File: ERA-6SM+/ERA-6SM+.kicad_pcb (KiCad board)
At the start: 2 copper layers, 60 x 30 mm, 91 parts, among them P1 CONN_01X02, U1 ERA-6+, X1 SMA-F, X2 SMA-F

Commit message: ERA-6SM+: Changed from 12V supply to 10V
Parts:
- R1: value 100 / 1W -> 69,8 / 0.5W
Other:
- board text added: "10V"
- board text removed: "12V"
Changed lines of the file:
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@@
 (kicad_pcb (version 4) (host pcbnew 4.0.2+e4-6225~38~ubuntu15.10.1-stable)
   (general
-    (links 99)
+    (links 97)
     (no_connects 0)
     (area 82.442143 88.535 180.275002 121.315)
@@
       (effects (font (size 1 1) (thickness 0.15)))
     )
-    (fp_text value "100 / 1W" (at 0 0) (layer F.Fab)
+    (fp_text value "69,8 / 0.5W" (at 0 0) (layer F.Fab)
       (effects (font (size 1 1) (thickness 0.15)))
     )
@@
       (net 1 GNDA))
   )
-  (gr_text 12V (at 112.38 111.223) (layer F.SilkS)
+  (gr_text 10V (at 112.38 111.223) (layer F.SilkS)
     (effects (font (size 1.5 1.5) (thickness 0.3)) (justify right))
   )

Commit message: ERA-6SM+: Table for bias resistor selection
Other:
- board text added: "43.2 69.8 100 127"
- board text added: "8 10 12 14"
- board text added: "R1"
- board text added: "VCC"
- board text removed: "10V"
- board text removed: "Leibniz Universität Hannover, GEM (EMV)"
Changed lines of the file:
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@@
     (area 82.442143 88.535 180.275002 121.315)
     (thickness 1.6)
-    (drawings 13)
+    (drawings 22)
     (tracks 18)
     (zones 0)
@@
     (tags "resistor 1206")
     (attr smd)
-    (fp_text reference R1 (at 3.302 0) (layer F.SilkS)
+    (fp_text reference R1 (at -0.127 2.032) (layer F.SilkS)
       (effects (font (size 1 1) (thickness 0.15)))
     )
@@
       (net 1 GNDA))
   )
-  (gr_text 10V (at 112.38 111.223) (layer F.SilkS)
+  (gr_text "8\n10\n12\n14" (at 128.255 113.89) (layer F.SilkS)
+    (effects (font (size 1 1) (thickness 0.15)) (justify left))
+  )
+  (gr_line (start 127.62 117.7) (end 136.51 117.7) (layer F.SilkS) (width 0.1))
+  (gr_line (start 127.62 110.08) (end 136.51 110.08) (layer F.SilkS) (width 0.1))
+  (gr_line (start 127.62 107.54) (end 136.51 107.54) (layer F.SilkS) (width 0.1))
+  (gr_line (start 136.51 107.54) (end 136.51 117.7) (layer F.SilkS) (width 0.1))
+  (gr_line (start 127.62 107.54) (end 127.62 117.7) (layer F.SilkS) (width 0.1))
+  (gr_line (start 132.065 107.54) (end 132.065 117.7) (layer F.SilkS) (width 0.1))
+  (gr_text "43.2\n69.8\n100\n127" (at 135.875 113.89) (layer F.SilkS)
+    (effects (font (size 1 1) (thickness 0.15)) (justify right))
+  )
+  (gr_text VCC (at 135.875 108.81) (layer F.SilkS)
+    (effects (font (size 1 1) (thickness 0.15)) (justify right))
+  )
+  (gr_text R1 (at 128.255 108.81) (layer F.SilkS)
+    (effects (font (size 1 1) (thickness 0.15)) (justify left))
+  )
+  (gr_text VCC (at 112.38 111.223) (layer F.SilkS)
     (effects (font (size 1.5 1.5) (thickness 0.3)) (justify right))
   )
@@
     (effects (font (size 1 1) (thickness 0.15)) (justify right))
   )
-  (gr_text "Leibniz Universität Hannover, GEM (EMV)" (at 120 117.446) (layer F.SilkS)
-    (effects (font (size 1 1) (thickness 0.15) italic))
-  )
   (gr_text ERA-6SM+ (at 100.1626 94.1796) (layer F.SilkS)

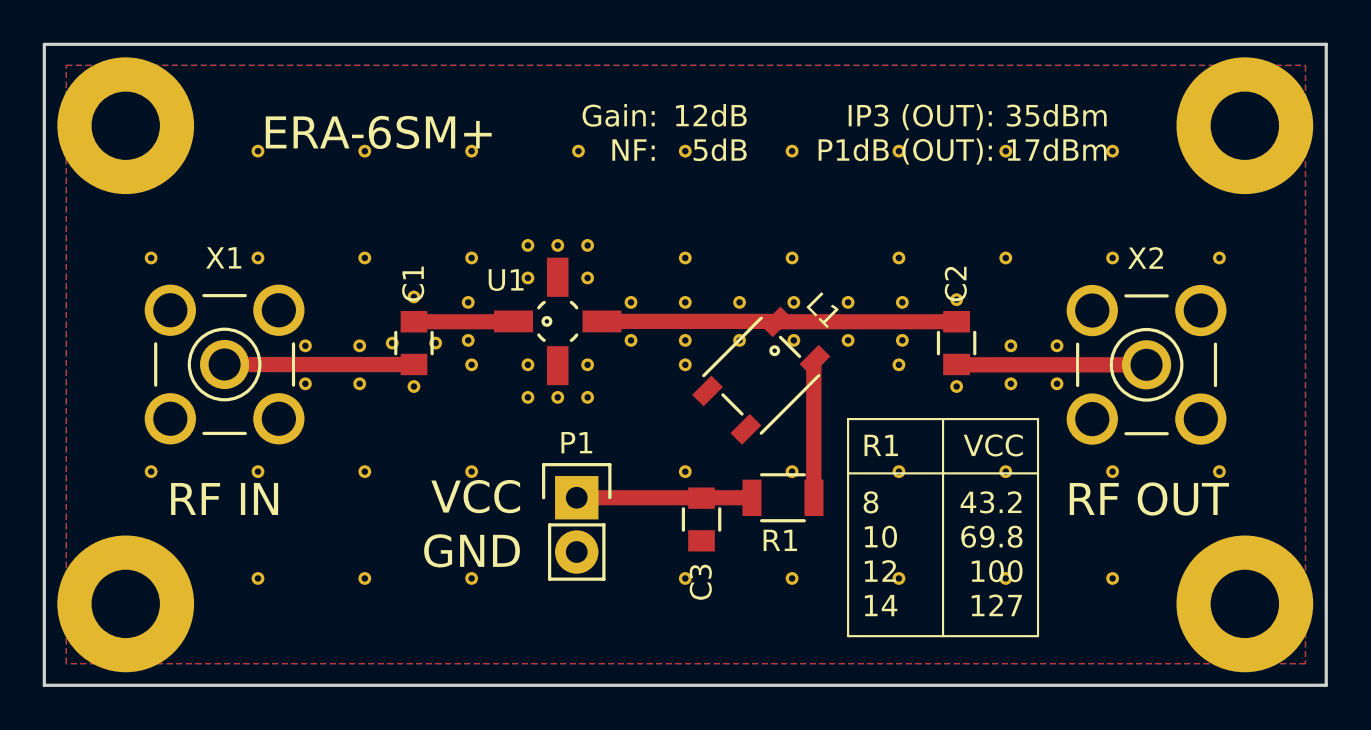
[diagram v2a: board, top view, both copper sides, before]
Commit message: ERA-6SM+: Corrected RF choke
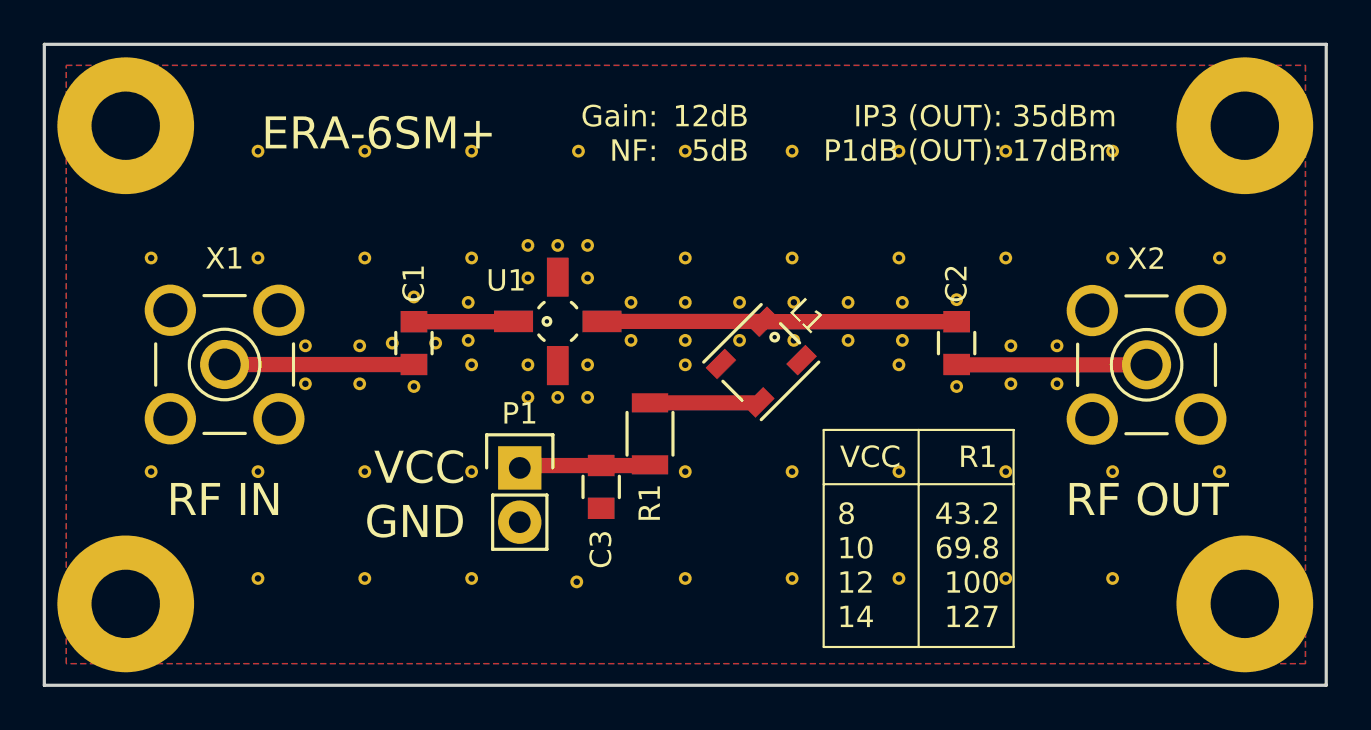
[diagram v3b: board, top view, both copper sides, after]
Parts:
- added REF**165: VIA-0.3, JueVias:VIA-0.3, F.Cu at (114.9, 115.2)
- moved R1 6.91 mm to (118.3, 108.2), turned to 90 degrees
- moved C3 4.94 mm to (116.1, 110.7)
- moved P1 3.01 mm to (112.3, 109.8)
- moved L1 0.63 mm to (123.6, 104.9)
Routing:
- net +12V: track 8.22 -> 6.21 mm
- net Net-(L1-Pad3): track 6.45 -> 5.13 mm
